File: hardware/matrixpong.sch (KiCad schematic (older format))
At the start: 325 parts

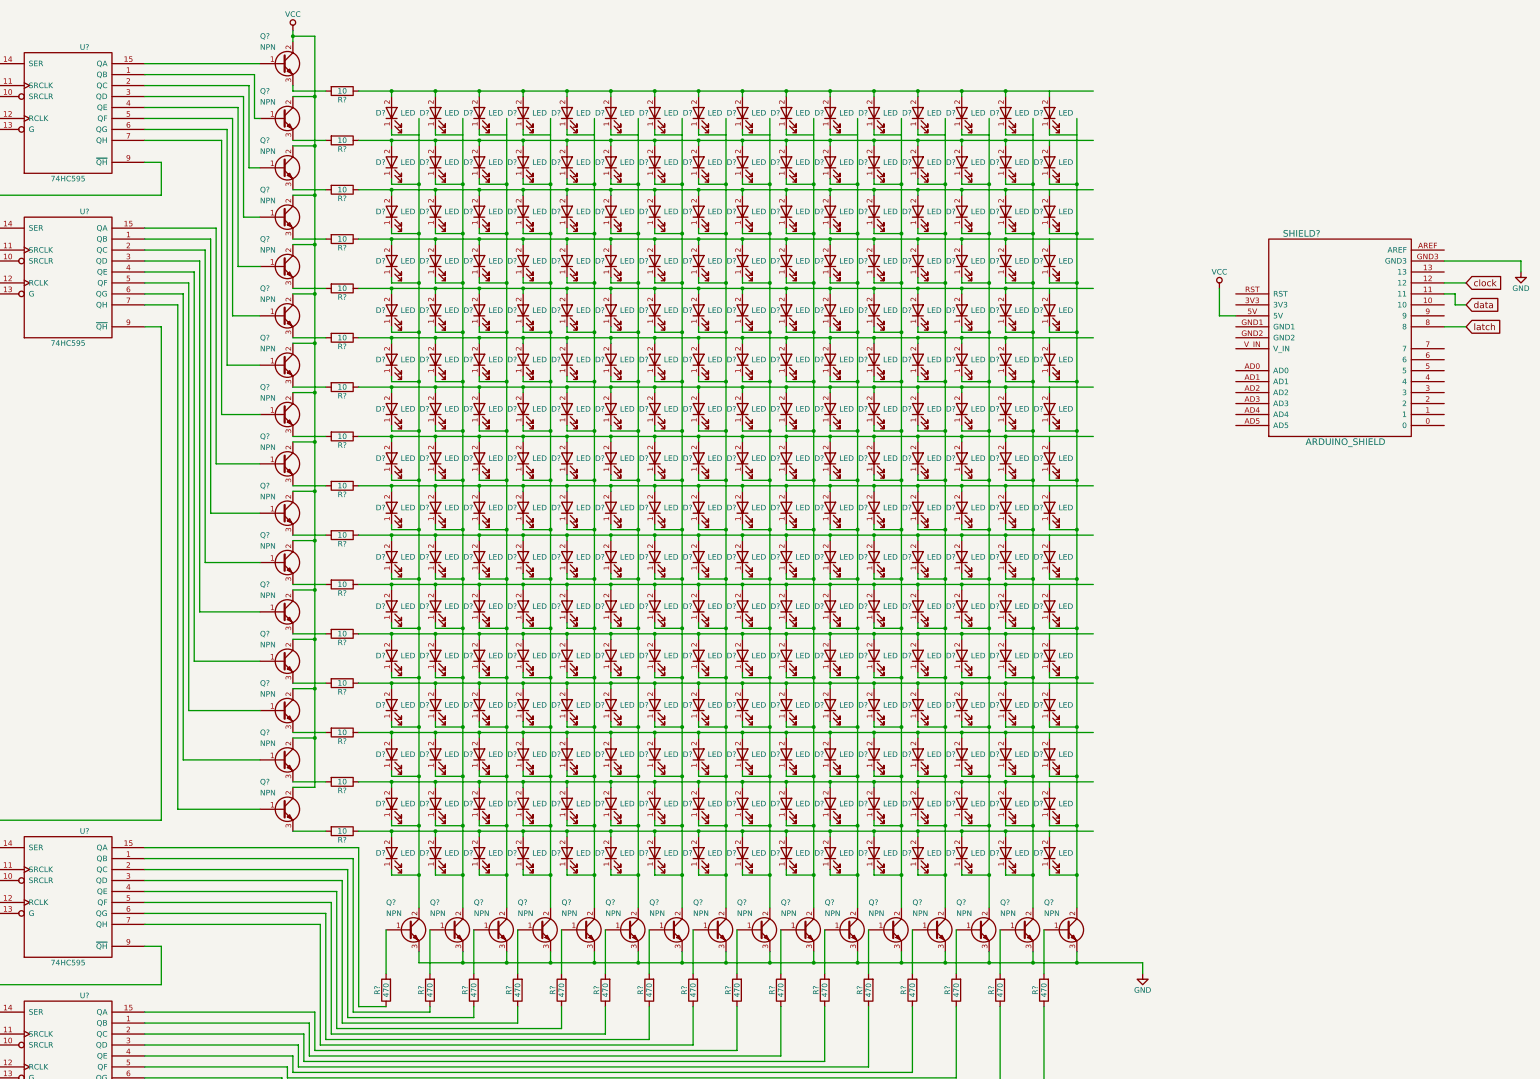
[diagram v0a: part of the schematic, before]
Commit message: enhanced matrix
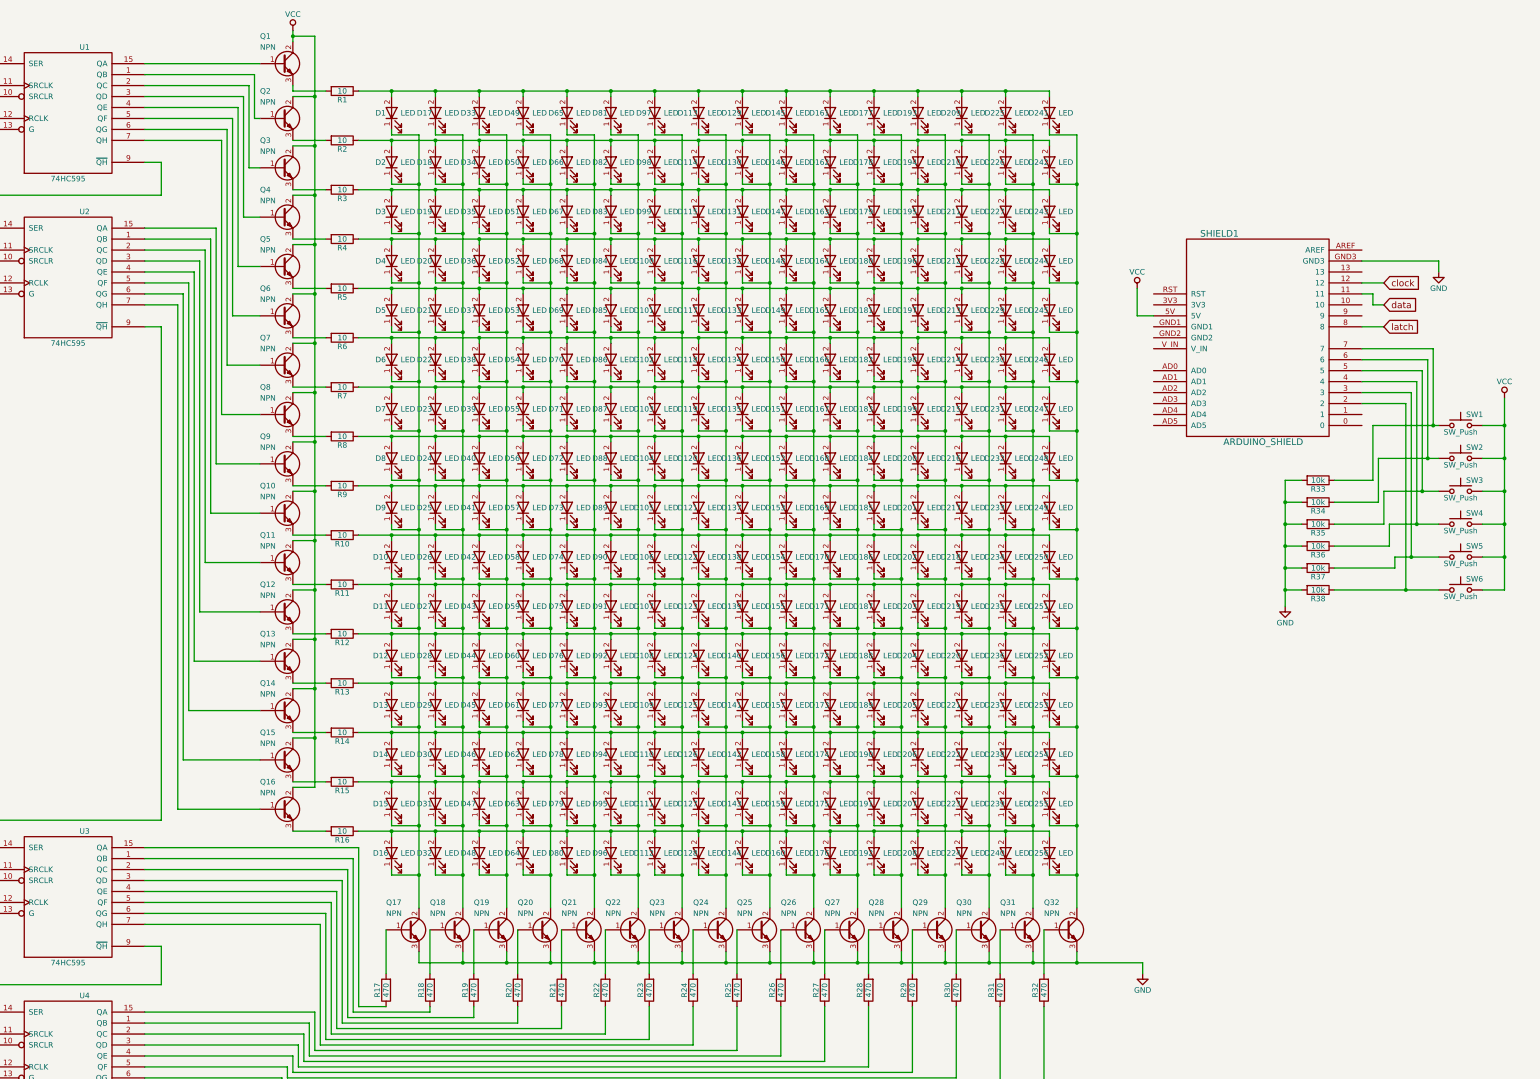
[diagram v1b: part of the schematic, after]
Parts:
- added R33, R34, R35, R36, R37, R38: 10k, Resistors_SMD:R_0805, symbol R
- added SW1, SW2, SW3, SW4, SW5, SW6: SW_Push, Buttons_Switches_SMD:SW_SPST_KMR2, symbol SW_Push
- D1, D10, D100, D101, D102, D103, D104, D105, D106, D107, D108, D109, D11, D110, D111, D112, D113, D114, D115, D116, D117, D118, D119, D12, D120, D121, D122, D123, D124, D125, D126, D127, D128, D129, D13, D130, D131, D132, D133, D134, D135, D136, D137, D138, D139, D14, D140, D141, D142, D143, D144, D145, D146, D147, D148, D149, D15, D150, D151, D152, D153, D154, D155, D156, D157, D158, D159, D16, D160, D161, D162, D163, D164, D165, D166, D167, D168, D169, D17, D170, D171, D172, D173, D174, D175, D176, D177, D178, D179, D18, D180, D181, D182, D183, D184, D185, D186, D187, D188, D189, D19, D190, D191, D192, D193, D194, D195, D196, D197, D198, D199, D2, D20, D200, D201, D202, D203, D204, D205, D206, D207, D208, D209, D21, D210, D211, D212, D213, D214, D215, D216, D217, D218, D219, D22, D220, D221, D222, D223, D224, D225, D226, D227, D228, D229, D23, D230, D231, D232, D233, D234, D235, D236, D237, D238, D239, D24, D240, D241, D242, D243, D244, D245, D246, D247, D248, D249, D25, D250, D251, D252, D253, D254, D255, D256, D26, D27, D28, D29, D3, D30, D31, D32, D33, D34, D35, D36, D37, D38, D39, D4, D40, D41, D42, D43, D44, D45, D46, D47, D48, D49, D5, D50, D51, D52, D53, D54, D55, D56, D57, D58, D59, D6, D60, D61, D62, D63, D64, D65, D66, D67, D68, D69, D7, D70, D71, D72, D73, D74, D75, D76, D77, D78, D79, D8, D80, D81, D82, D83, D84, D85, D86, D87, D88, D89, D9, D90, D91, D92, D93, D94, D95, D96, D97, D98, D99: renamed from D?; footprint (none) -> LEDs:LED_0603
- Q1, Q10, Q11, Q12, Q13, Q14, Q15, Q16, Q17, Q18, Q19, Q2, Q20, Q21, Q22, Q23, Q24, Q25, Q26, Q27, Q28, Q29, Q3, Q30, Q31, Q32, Q4, Q5, Q6, Q7, Q8, Q9: renamed from Q?; footprint (none) -> TO_SOT_Packages_SMD:SOT-23
- R1, R10, R11, R12, R13, R14, R15, R16, R17, R18, R19, R2, R20, R21, R22, R23, R24, R25, R26, R27, R28, R29, R3, R30, R31, R32, R4, R5, R6, R7, R8, R9: renamed from R?; footprint (none) -> Resistors_SMD:R_0805
- SHIELD1: renamed from SHIELD?; footprint (none) -> arduino_shields:ARDUINO SHIELD
- U1, U2, U3, U4: renamed from U?; footprint (none) -> Housings_DIP:DIP-16_W7.62mm
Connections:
- wire segments 1025 -> 1067
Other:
- moved on the sheet: SHIELD1

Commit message: changed resistor to emmitter line and added components list
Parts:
- Q1, Q10, Q11, Q12, Q13, Q14, Q15, Q16, Q17, Q18, Q19, Q2, Q20, Q21, Q22, Q23, Q24, Q25, Q26, Q27, Q28, Q29, Q3, Q30, Q31, Q32, Q4, Q5, Q6, Q7, Q8, Q9: symbol Q_NPN_BCE -> Q_NPN_BEC
- R1, R10, R11, R12, R13, R14, R15, R16, R2, R3, R4, R5, R6, R7, R8, R9: value 10 -> 47
- U1, U2, U3, U4: footprint Housings_DIP:DIP-16_W7.62mm -> SMD_Packages:SO-16-N
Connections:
- net GND: now also Q17.2 (E), Q18.2 (E), Q19.2 (E), Q20.2 (E), Q21.2 (E), Q22.2 (E), Q23.2 (E), Q24.2 (E), Q25.2 (E), Q26.2 (E), Q27.2 (E), Q28.2 (E), Q29.2 (E), Q30.2 (E), Q31.2 (E), Q32.2 (E); no longer Q17.3 (E), Q18.3 (E), Q19.3 (E), Q20.3 (E), Q21.3 (E), Q22.3 (E), Q23.3 (E), Q24.3 (E), Q25.3 (E), Q26.3 (E), Q27.3 (E), Q28.3 (E), Q29.3 (E), Q30.3 (E), Q31.3 (E), Q32.3 (E)
- net VCC: now also Q1.3 (C), Q10.3 (C), Q11.3 (C), Q12.3 (C), Q13.3 (C), Q14.3 (C), Q15.3 (C), Q16.3 (C), Q2.3 (C), Q3.3 (C), Q4.3 (C), Q5.3 (C), Q6.3 (C), Q7.3 (C), Q8.3 (C), Q9.3 (C); no longer Q1.2 (C), Q10.2 (C), Q11.2 (C), Q12.2 (C), Q13.2 (C), Q14.2 (C), Q15.2 (C), Q16.2 (C), Q2.2 (C), Q3.2 (C), Q4.2 (C), Q5.2 (C), Q6.2 (C), Q7.2 (C), Q8.2 (C), Q9.2 (C)
- net at D1.1 (K), D10.1 (K), D11.1 (K)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: now also R1.2; no longer Q17.2 (C)
- net at D1.2 (A), D113.2 (A), D129.2 (A)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: now also Q1.2 (E); no longer R1.1
- net at D17.1 (K), D18.1 (K), D19.1 (K)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: now also R2.2; no longer Q18.2 (C)
- net at D33.1 (K), D34.1 (K), D35.1 (K)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: now also R3.2; no longer Q19.2 (C)
- net at D49.1 (K), D50.1 (K), D51.1 (K)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: now also R4.2; no longer Q20.2 (C)
- net at D65.1 (K), D66.1 (K), D67.1 (K)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: now also R5.2; no longer Q21.2 (C)
- net at D81.1 (K), D82.1 (K), D83.1 (K)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: now also R6.2; no longer Q22.2 (C)
- net at D100.1 (K), D101.1 (K), D102.1 (K)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: now also R7.2; no longer Q23.2 (C)
- net at D113.1 (K), D114.1 (K), D115.1 (K)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: now also R8.2; no longer Q24.2 (C)
- net at D129.1 (K), D130.1 (K), D131.1 (K)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: now also R9.2; no longer Q25.2 (C)
- net at D145.1 (K), D146.1 (K), D147.1 (K)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: now also R10.2; no longer Q26.2 (C)
- net at D161.1 (K), D162.1 (K), D163.1 (K)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: now also R11.2; no longer Q27.2 (C)
- net at D177.1 (K), D178.1 (K), D179.1 (K)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: now also R12.2; no longer Q28.2 (C)
- net at D193.1 (K), D194.1 (K), D195.1 (K)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: now also R13.2; no longer Q29.2 (C)
- net at D209.1 (K), D210.1 (K), D211.1 (K)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: now also R14.2; no longer Q30.2 (C)
- net at D225.1 (K), D226.1 (K), D227.1 (K)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: now also R15.2; no longer Q31.2 (C)
- net at D241.1 (K), D242.1 (K), D243.1 (K)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: now also R16.2; no longer Q32.2 (C)
- net at D114.2 (A), D130.2 (A), D146.2 (A)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: now also Q2.2 (E); no longer R2.1
- net at D115.2 (A), D131.2 (A), D147.2 (A)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: now also Q3.2 (E); no longer R3.1
- net at D100.2 (A), D116.2 (A), D132.2 (A)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: now also Q4.2 (E); no longer R4.1
- net at D101.2 (A), D117.2 (A), D133.2 (A)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: now also Q5.2 (E); no longer R5.1
- net at D102.2 (A), D118.2 (A), D134.2 (A)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: now also Q6.2 (E); no longer R6.1
- net at D103.2 (A), D119.2 (A), D135.2 (A)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: now also Q7.2 (E); no longer R7.1
- net at D104.2 (A), D120.2 (A), D136.2 (A)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: now also Q8.2 (E); no longer R8.1
- net at D105.2 (A), D121.2 (A), D137.2 (A)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: now also Q9.2 (E); no longer R9.1
- net at D10.2 (A), D106.2 (A), D122.2 (A)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: now also Q10.2 (E); no longer R10.1
- net at D107.2 (A), D11.2 (A), D123.2 (A)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: now also Q11.2 (E); no longer R11.1
- net at D108.2 (A), D12.2 (A), D124.2 (A)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: now also Q12.2 (E); no longer R12.1
- net at D109.2 (A), D125.2 (A), D13.2 (A)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: now also Q13.2 (E); no longer R13.1
- net at D110.2 (A), D126.2 (A), D14.2 (A)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: now also Q14.2 (E); no longer R14.1
- net at D111.2 (A), D127.2 (A), D143.2 (A)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: now also Q15.2 (E); no longer R15.1
- net at D112.2 (A), D128.2 (A), D144.2 (A)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: now also Q16.2 (E); no longer R16.1
- new net: Q17.3 (C), R1.1
- new net: Q18.3 (C), R2.1
- new net: Q19.3 (C), R3.1
- new net: Q20.3 (C), R4.1
- new net: Q21.3 (C), R5.1
- new net: Q22.3 (C), R6.1
- new net: Q23.3 (C), R7.1
- new net: Q24.3 (C), R8.1
- new net: Q25.3 (C), R9.1
- new net: Q26.3 (C), R10.1
- new net: Q27.3 (C), R11.1
- new net: Q28.3 (C), R12.1
- new net: Q29.3 (C), R13.1
- new net: Q30.3 (C), R14.1
- new net: Q31.3 (C), R15.1
- new net: Q32.3 (C), R16.1
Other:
- moved on the sheet: D1, D10, D100, D101, D102, D103, D104, D105, D106, D107, D108, D109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
